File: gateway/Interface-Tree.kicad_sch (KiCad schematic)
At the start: 0 parts

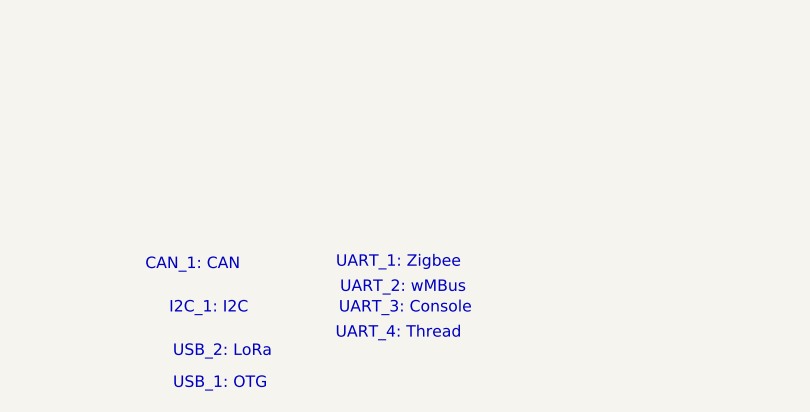
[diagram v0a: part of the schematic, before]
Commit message: Add ready LED, swap Zigbee and Console UART
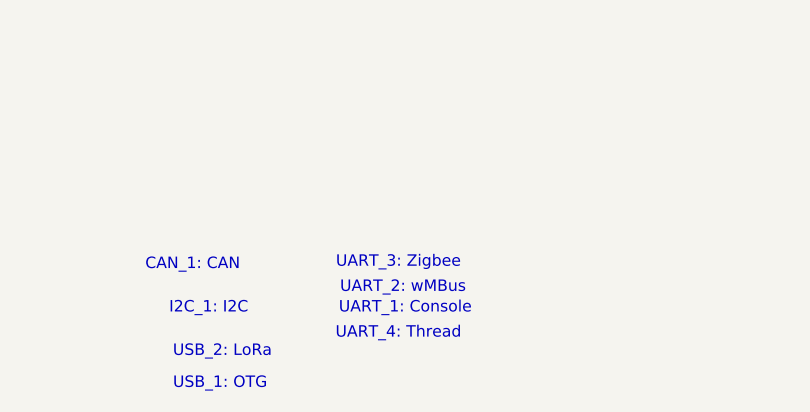
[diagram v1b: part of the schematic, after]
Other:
- note added: "UART_1: Console"
- note added: "UART_3: Zigbee"
- note removed: "UART_1: Zigbee"
- note removed: "UART_3: Console"
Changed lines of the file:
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@@
 		)
 	)
-	(text "UART_1: Zigbee"
+	(text "UART_3: Zigbee"
 		(exclude_from_sim no)
 		(at 220.98 171.704 0)
@@
 		)
 	)
-	(text "UART_3: Console"
+	(text "UART_1: Console"
 		(exclude_from_sim no)
 		(at 221.742 176.784 0)
@@
 			2.54 2.54 2.54 2.54 2.54 2.54 2.54 2.54 2.54 2.54 2.54 2.54 2.54 2.54
 			2.54 2.54 2.54 2.54 2.54 2.54 2.54 2.54 2.54 2.54 2.54 2.54 2.54 2.54
-			2.54
+			2.54 2.54
 		)
 		(cells
@@
 				)
 			)
-			(table_cell "PowerMux-Status"
+			(table_cell "LED Ready"
 				(exclude_from_sim no)
 				(at 13.97 215.9 0)
@@
 				)
 			)
-			(table_cell "210"
+			(table_cell "206"
 				(exclude_from_sim no)
 				(at 43.18 215.9 0)
@@
 				)
 			)
-			(table_cell "PWR_1V8_MOCI"
+			(table_cell "PowerMux-Status"
 				(exclude_from_sim no)
 				(at 13.97 218.44 0)
@@
 				)
 			)
-			(table_cell "214"
+			(table_cell "210"
 				(exclude_from_sim no)
 				(at 43.18 218.44 0)
@@
 				)
 			)
-			(table_cell "Ethernet.TRD0_P"
+			(table_cell "PWR_1V8_MOCI"
 				(exclude_from_sim no)
 				(at 13.97 220.98 0)
@@
 				)
 			)
-			(table_cell "225"
+			(table_cell "214"
 				(exclude_from_sim no)
 				(at 43.18 220.98 0)
@@
 				)
 			)
-			(table_cell "PCIe.CLK_N"
+			(table_cell "Ethernet.TRD0_P"
 				(exclude_from_sim no)
 				(at 13.97 223.52 0)
@@
 				)
 			)
-			(table_cell "226"
+			(table_cell "225"
 				(exclude_from_sim no)
 				(at 43.18 223.52 0)
@@
 				)
 			)
-			(table_cell "Ethernet.TRD0_N"
+			(table_cell "PCIe.CLK_N"
 				(exclude_from_sim no)
 				(at 13.97 226.06 0)
@@
 				)
 			)
-			(table_cell "227"
+			(table_cell "226"
 				(exclude_from_sim no)
 				(at 43.18 226.06 0)
@@
 				)
 			)
-			(table_cell "PCIe.CLK_P"
+			(table_cell "Ethernet.TRD0_N"
 				(exclude_from_sim no)
 				(at 13.97 228.6 0)
@@
 				)
 			)
-			(table_cell "228"
+			(table_cell "227"
 				(exclude_from_sim no)
 				(at 43.18 228.6 0)
@@
 				)
 			)
-			(table_cell "Ethernet.TRD1_N"
+			(table_cell "PCIe.CLK_P"
 				(exclude_from_sim no)
 				(at 13.97 231.14 0)
@@
 				)
 			)
-			(table_cell "231"
+			(table_cell "228"
 				(exclude_from_sim no)
 				(at 43.18 231.14 0)
@@
 				)
 			)
-			(table_cell "PCIe.RX_P"
+			(table_cell "Ethernet.TRD1_N"
 				(exclude_from_sim no)
 				(at 13.97 233.68 0)
@@
 				)
 			)
-			(table_cell "234"
+			(table_cell "231"
 				(exclude_from_sim no)
 				(at 43.18 233.68 0)
@@
 				)
 			)
-			(table_cell "Ethernet.TRD1_P"
+			(table_cell "PCIe.RX_P"
 				(exclude_from_sim no)
 				(at 13.97 236.22 0)
@@
 				)
 			)
-			(table_cell "233"
+			(table_cell "234"
 				(exclude_from_sim no)
 				(at 43.18 236.22 0)
@@
 				)
 			)
-			(table_cell "Ethernet.LED-Yellow"
+			(table_cell "Ethernet.TRD1_P"
 				(exclude_from_sim no)
 				(at 13.97 238.76 0)
@@
 				)
 			)
-			(table_cell "235"
+			(table_cell "233"
 				(exclude_from_sim no)
 				(at 43.18 238.76 0)
@@
 				)
 			)
-			(table_cell "PCIe.RX_N"
+			(table_cell "Ethernet.LED-Yellow"
 				(exclude_from_sim no)
 				(at 13.97 241.3 0)
@@
 				)
 			)
-			(table_cell "236"
+			(table_cell "235"
 				(exclude_from_sim no)
 				(at 43.18 241.3 0)
@@
 				)
 			)
-			(table_cell "Ethernet.LED-Green"
+			(table_cell "PCIe.RX_N"
 				(exclude_from_sim no)
 				(at 13.97 243.84 0)
@@
 				)
 			)
-			(table_cell "237"
+			(table_cell "236"
 				(exclude_from_sim no)
 				(at 43.18 243.84 0)
@@
 				)
 			)
-			(table_cell "PCIe.TX_P"
+			(table_cell "Ethernet.LED-Green"
 				(exclude_from_sim no)
 				(at 13.97 246.38 0)
@@
 				)
 			)
-			(table_cell "238"
+			(table_cell "237"
 				(exclude_from_sim no)
 				(at 43.18 246.38 0)
@@
 				)
 			)
-			(table_cell "Ethernet.TRD2_P"
+			(table_cell "PCIe.TX_P"
 				(exclude_from_sim no)
 				(at 13.97 248.92 0)
@@
 				)
 			)
-			(table_cell "239"
+			(table_cell "238"
 				(exclude_from_sim no)
 				(at 43.18 248.92 0)
@@
 				)
 			)
-			(table_cell "PCIe.TX_N"
+			(table_cell "Ethernet.TRD2_P"
 				(exclude_from_sim no)
 				(at 13.97 251.46 0)
@@
 				)
 			)
-			(table_cell "240"
+			(table_cell "239"
 				(exclude_from_sim no)
 				(at 43.18 251.46 0)
@@
 				)
 			)
-			(table_cell "Ethernet.TRD2_N"
+			(table_cell "PCIe.TX_N"
 				(exclude_from_sim no)
 				(at 13.97 254 0)
@@
 				)
 			)
-			(table_cell "241"
+			(table_cell "240"
 				(exclude_from_sim no)
 				(at 43.18 254 0)
@@
 				)
 			)
-			(table_cell "PCIe.RST"
+			(table_cell "Ethernet.TRD2_N"
 				(exclude_from_sim no)
 				(at 13.97 256.54 0)
@@
 				)
 			)
-			(table_cell "244"
+			(table_cell "241"
 				(exclude_from_sim no)
 				(at 43.18 256.54 0)
@@
 				)
 			)
-			(table_cell "Ethernet.TRD3_N"
+			(table_cell "PCIe.RST"
 				(exclude_from_sim no)
 				(at 13.97 259.08 0)
@@
 				)
 			)
-			(table_cell "245"
+			(table_cell "244"
 				(exclude_from_sim no)
 				(at 43.18 259.08 0)
@@
 				)
 			)
-			(table_cell "CTRL_RECOVERY_MICO"
+			(table_cell "Ethernet.TRD3_N"
 				(exclude_from_sim no)
 				(at 13.97 261.62 0)
@@
 				)
 			)
-			(table_cell "246"
+			(table_cell "245"
 				(exclude_from_sim no)
 				(at 43.18 261.62 0)
@@
 				)
 			)
-			(table_cell "Ethernet.TRD3_P"
+			(table_cell "CTRL_RECOVERY_MICO"
 				(exclude_from_sim no)
 				(at 13.97 264.16 0)
@@
 				)
 			)
-			(table_cell "247"
+			(table_cell "246"
 				(exclude_from_sim no)
 				(at 43.18 264.16 0)
@@
 				)
 			)
-			(table_cell "CTRL_PWR_BTN_MICO"
+			(table_cell "Ethernet.TRD3_P"
 				(exclude_from_sim no)
 				(at 13.97 266.7 0)
@@
 				)
 			)
-			(table_cell "248"
+			(table_cell "247"
 				(exclude_from_sim no)
 				(at 43.18 266.7 0)
@@
 				)
 			)
-			(table_cell "CTRL_FORCE_OFF_MOCI"
+			(table_cell "CTRL_PWR_BTN_MICO"
 				(exclude_from_sim no)
 				(at 13.97 269.24 0)
@@
 				)
 			)
-			(table_cell "250"
+			(table_cell "248"
 				(exclude_from_sim no)
 				(at 43.18 269.24 0)
@@
 				)
 			)
-			(table_cell "CTRL_WAKE1_MICO"
+			(table_cell "CTRL_FORCE_OFF_MOCI"
 				(exclude_from_sim no)
 				(at 13.97 271.78 0)
@@
 				)
 			)
-			(table_cell "252"
+			(table_cell "250"
 				(exclude_from_sim no)
 				(at 43.18 271.78 0)
@@
 				)
 			)
-			(table_cell "SoM-Power-Enable"
+			(table_cell "CTRL_WAKE1_MICO"
 				(exclude_from_sim no)
 				(at 13.97 274.32 0)
@@
 				)
 			)
-			(table_cell "254"
+			(table_cell "252"
 				(exclude_from_sim no)
 				(at 43.18 274.32 0)
@@
 				)
 			)
-			(table_cell "CTRL_RESET_MOCI"
+			(table_cell "SoM-Power-Enable"
 				(exclude_from_sim no)
 				(at 13.97 276.86 0)
@@
 				)
 			)
-			(table_cell "258"
+			(table_cell "254"
 				(exclude_from_sim no)
 				(at 43.18 276.86 0)
@@
 				)
 			)
-			(table_cell "CTRL_RESET_MICO"
+			(table_cell "CTRL_RESET_MOCI"
 				(exclude_from_sim no)
 				(at 13.97 279.4 0)
@@
 				)
 			)
-			(table_cell "260"
+			(table_cell "258"
 				(exclude_from_sim no)
 				(at 43.18 279.4 0)
@@
 				(size 0 2.54)
 				(margins 0.9525 0.9525 0.9525 0.9525)
+				(span 1 1)
+				(fill
+					(type none)
+				)
+				(effects
+					(font
+						(size 1.27 1.27)
+					)
+					(justify left top)
+				)
+			)
+			(table_cell "CTRL_RESET_MICO"
+				(exclude_from_sim no)
+				(at 13.97 281.94 0)
+				(size 29.21 2.54)
+				(margins 0.9525 0.9525 0.9525 0.9525)
+				(span 1 1)
+				(fill
+					(type none)
+				)
+				(effects
+					(font
+						(size 1.27 1.27)
+					)
+					(justify left top)
+				)
+			)
+			(table_cell "260"
+				(exclude_from_sim no)
+				(at 43.18 281.94 0)
+				(size 22.86 2.54)
+				(margins 0.9525 0.9525 0.9525 0.9525)
+				(span 1 1)
+				(fill
+					(type none)
+				)
+				(effects
+					(font
+						(size 1.27 1.27)
+					)
+					(justify left top)
+				)
+			)
+			(table_cell ""
+				(exclude_from_sim no)
+				(at 66.04 281.94 0)
+				(size 0 2.54)
+				(margins 0.9525 0.9525 0.9525 0.9525)

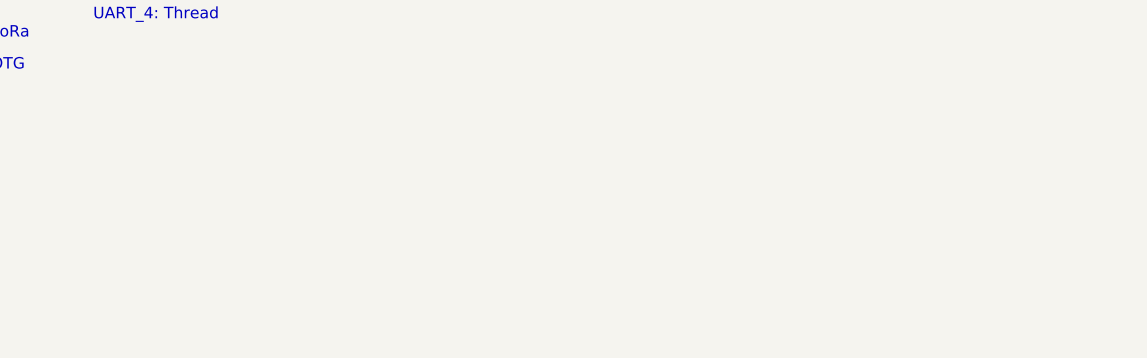
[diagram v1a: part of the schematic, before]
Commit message: Add INA219 for current measurement
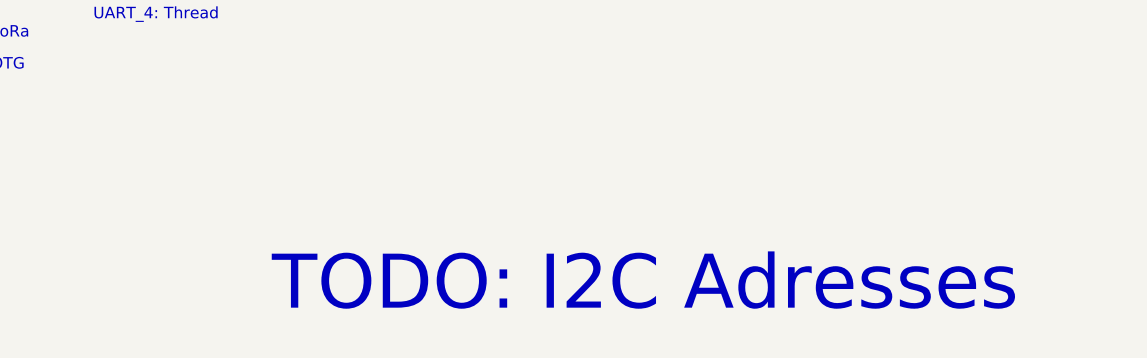
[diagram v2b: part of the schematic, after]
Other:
- note added: "TODO: I2C Adresses"
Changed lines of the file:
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@@
 	(title_block
 		(title "Interface - Tree")
-		(date "2025-06-05")
+		(date "2026-07-09")
 		(rev "${REVISION}")
 		(company "${COMPANY}")
 	)
+	(text "TODO: I2C Adresses"
+		(exclude_from_sim no)
+		(at 275.336 209.55 0)
+		(effects
+			(font
+				(size 6 6)
+			)
+		)
+	)
 	(text "I2C_1: I2C"
 		(exclude_from_sim no)
@@
 				)
 			)
-			(table_cell "Zigbee.RxD"
+			(table_cell "Console-RxD"
 				(exclude_from_sim no)
 				(at 13.97 167.64 0)
@@
 				)
 			)
-			(table_cell "Zigbee.TxD"
+			(table_cell "Console-TxD"
 				(exclude_from_sim no)
 				(at 13.97 170.18 0)
@@
 				)
 			)
-			(table_cell "Console-RxD"
+			(table_cell "Zigbee.RxD"
 				(exclude_from_sim no)
 				(at 13.97 177.8 0)
@@
 				)
 			)
-			(table_cell "Console-TxD"
+			(table_cell "Zigbee.TxD"
 				(exclude_from_sim no)
 				(at 13.97 180.34 0)

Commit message: Add boot signal for Thread MCU
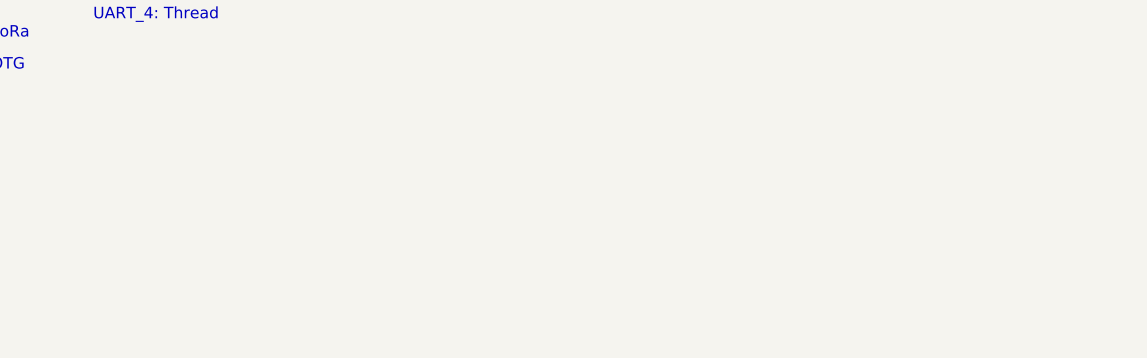
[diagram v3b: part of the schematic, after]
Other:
- note removed: "TODO: I2C Adresses"

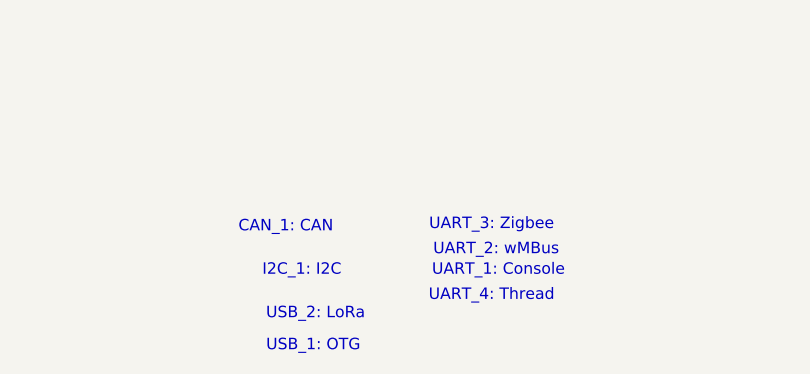
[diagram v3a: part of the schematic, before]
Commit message: Improving Thread
- Add boot signal for Thread MCU
- Add debug LED for nRF5340
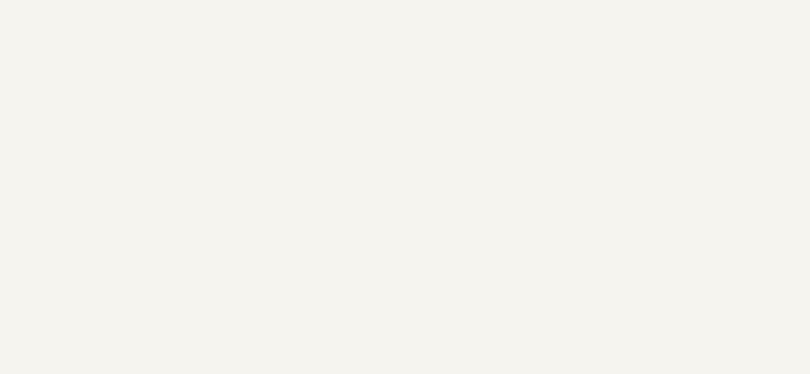
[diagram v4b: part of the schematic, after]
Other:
- note removed: "CAN_1: CAN"
- note removed: "I2C_1: I2C"
- note removed: "UART_1: Console"
- note removed: "UART_2: wMBus"
- note removed: "UART_3: Zigbee"
- note removed: "UART_4: Thread"
- note removed: "USB_1: OTG"
- note removed: "USB_2: LoRa"
